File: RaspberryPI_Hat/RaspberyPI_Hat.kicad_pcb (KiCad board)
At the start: 2 copper layers, 65 x 56 mm, 45 parts, among them Q1 BC817, Q2 BC817, Q3 BC817, SW1 SW_PUSH, U1 CAT24C32WI-GT3

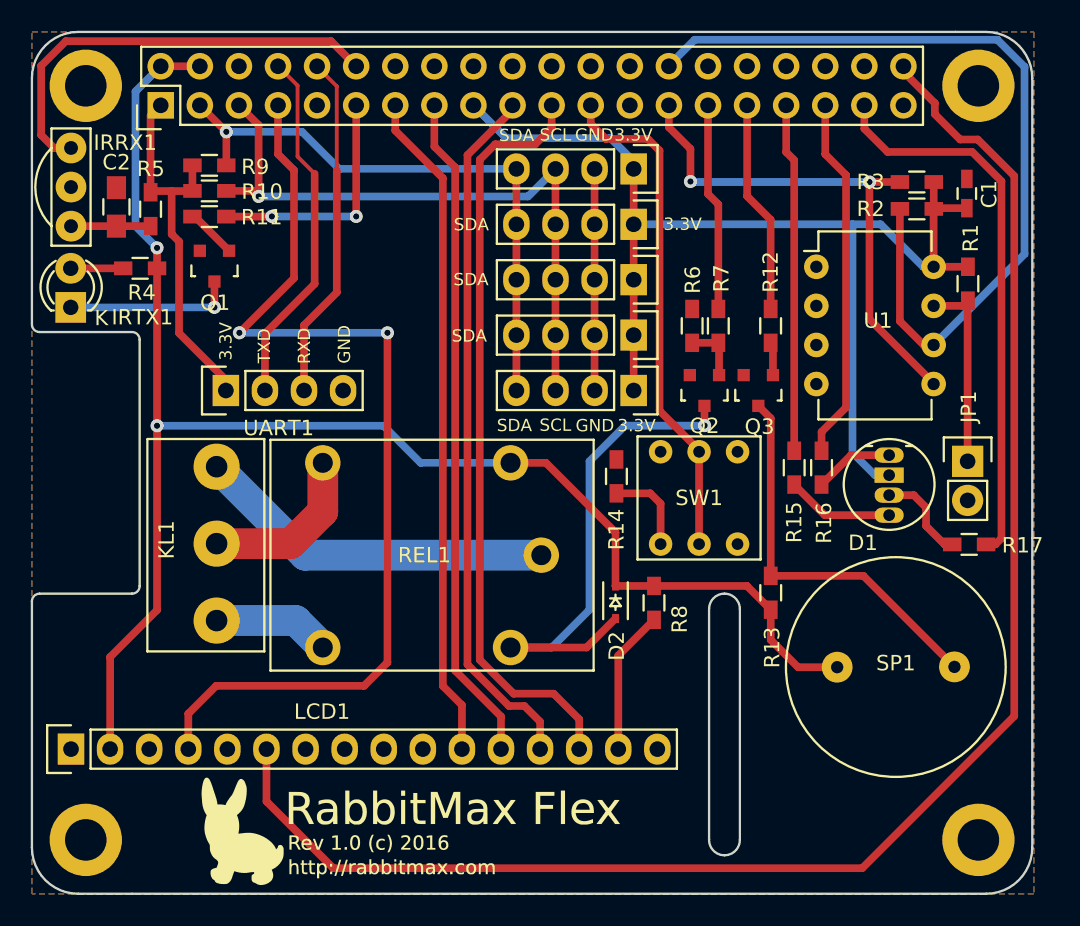
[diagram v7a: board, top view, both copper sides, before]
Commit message: changed common A to common Katode RGB LED
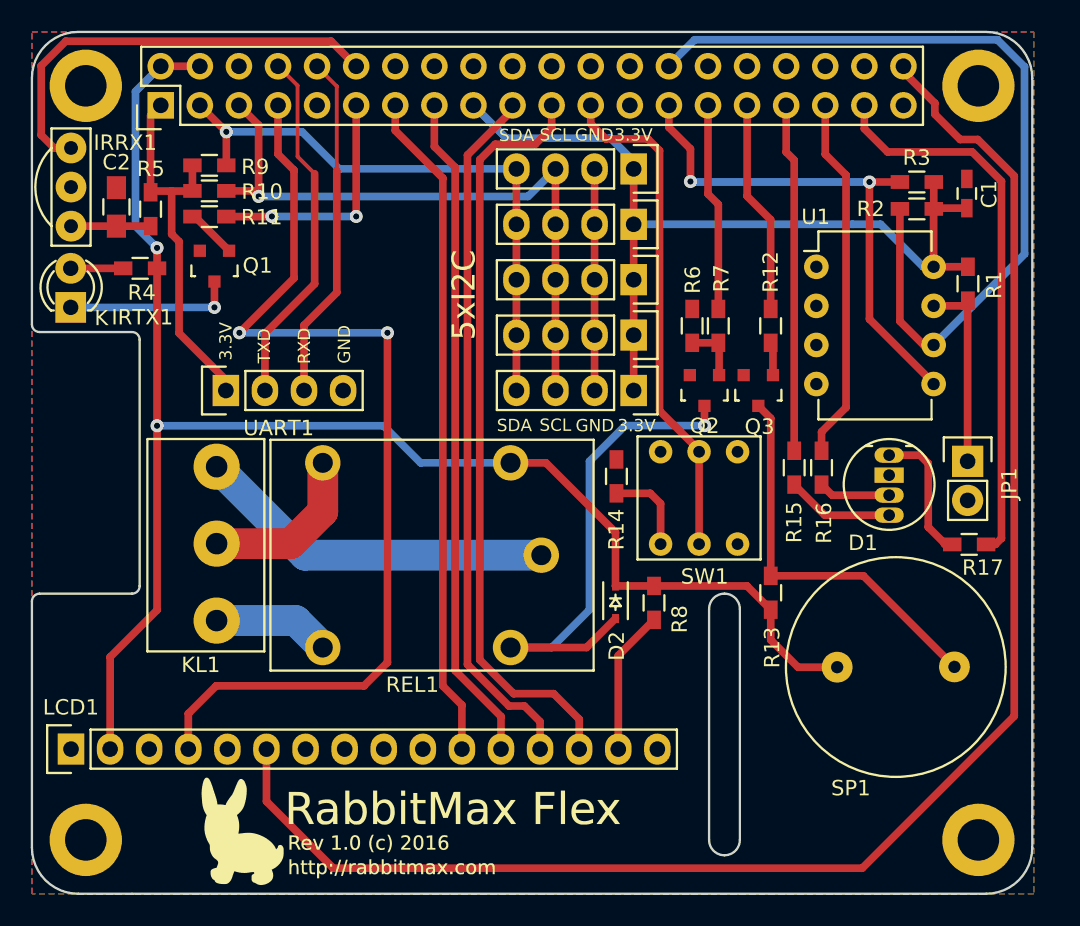
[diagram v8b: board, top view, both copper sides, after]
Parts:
- D1: value LED_RABG -> LED_RCBG
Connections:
- D1 pad 2: +3V3 -> GND
- R16 pad 2: Net-(D1-Pad1) -> Net-(D1-Pad3)
- R17 pad 1: Net-(D1-Pad3) -> Net-(D1-Pad1)
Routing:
- net +3V3: track 99.9 -> 82.1 mm
- net Net-(D1-Pad1): track 5.18 -> 9.42 mm
- net Net-(D1-Pad3): track 6.13 -> 4.68 mm
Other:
- board text added: "5xI2C"
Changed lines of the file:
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@@
     (links 110)
     (no_connects 2)
-    (area 97.924999 68.524999 163.075001 124.675001)
+    (area 86.242429 56.842428 174.757572 125.479)
     (thickness 1.6)
-    (drawings 44)
-    (tracks 265)
+    (drawings 41)
+    (tracks 263)
     (zones 0)
     (modules 45)
@@
       (effects (font (size 1 1) (thickness 0.15)))
     )
-    (fp_text value LED_RABG (at 0 6.25) (layer F.Fab)
+    (fp_text value LED_RCBG (at 0 6.25) (layer F.Fab)
       (effects (font (size 1 1) (thickness 0.15)))
     )
@@
       (net 43 "Net-(D1-Pad1)"))
     (pad 2 thru_hole rect (at 0 1.3) (size 1.905 1) (drill 0.762) (layers *.Cu *.Mask F.SilkS)
-      (net 2 +3V3))
+      (net 1 GND))
     (pad 3 thru_hole oval (at 0 2.6) (size 1.905 1) (drill 0.762) (layers *.Cu *.Mask F.SilkS)
       (net 44 "Net-(D1-Pad3)"))
@@
   (module myfootprint:PUSH_P1 (layer F.Cu)
     (at 141.35 98.88)
-    (fp_text reference SW1 (at 0 0) (layer F.SilkS)
+    (fp_text reference SW1 (at 0.36 5.11) (layer F.SilkS)
       (effects (font (size 1 1) (thickness 0.15)))
     )
@@
     (tags SOT-23)
     (attr smd)
-    (fp_text reference Q1 (at -0.04 -2.38 360) (layer F.SilkS)
+    (fp_text reference Q1 (at -2.8 0.04 360) (layer F.SilkS)
       (effects (font (size 1 1) (thickness 0.15)))
     )
@@
   (module myfootprint:PIEZO-MCKPI-G1410 (layer F.Cu)
     (at 154.134 109.868)
-    (fp_text reference SP1 (at 0 -0.25) (layer F.SilkS)
+    (fp_text reference SP1 (at -2.924 7.872) (layer F.SilkS)
       (effects (font (size 1 1) (thickness 0.15)))
     )
@@
     (tags "resistor 0603")
     (attr smd)
-    (fp_text reference R1 (at -2.96 -0.18 270) (layer F.SilkS)
+    (fp_text reference R1 (at 0.08 -1.7 270) (layer F.SilkS)
       (effects (font (size 1 1) (thickness 0.15)))
     )
@@
     (tags "resistor 0603")
     (attr smd)
-    (fp_text reference R3 (at 3 0 180) (layer F.SilkS)
+    (fp_text reference R3 (at 0.01 1.58 180) (layer F.SilkS)
       (effects (font (size 1 1) (thickness 0.15)))
     )
@@
     (descr "Through hole pin header")
     (tags "pin header")
-    (fp_text reference JP1 (at 0.08 -3.54 90) (layer F.SilkS)
+    (fp_text reference JP1 (at 2.71 1.46 90) (layer F.SilkS)
       (effects (font (size 1 1) (thickness 0.15)))
     )
@@
     (descr "8-lead dip package, row spacing 7.62 mm (300 mils)")
     (tags "dil dip 2.54 300")
-    (fp_text reference U1 (at 4 3.5) (layer F.SilkS)
+    (fp_text reference U1 (at -0.04 -3.24) (layer F.SilkS)
       (effects (font (size 1 1) (thickness 0.15)))
     )
@@
       (net 19 /LED1))
     (pad 2 smd rect (at 1.1 0 270) (size 1.2 0.9) (layers F.Cu F.Paste F.Mask)
-      (net 43 "Net-(D1-Pad1)"))
+      (net 44 "Net-(D1-Pad3)"))
     (model Resistors_SMD.3dshapes/R_0603_HandSoldering.wrl
       (at (xyz 0 0 0))
@@
   (module myfootprint:KLEMA_1x3 (layer F.Cu)
     (at 113.5 96.85 270)
-    (fp_text reference KL1 (at 4.75 6.75 270) (layer F.SilkS)
+    (fp_text reference KL1 (at 12.88 4.53 360) (layer F.SilkS)
       (effects (font (size 1 1) (thickness 0.15)))
     )
@@
   (module myfootprint:RAS-05-15 (layer F.Cu)
     (at 119 95.1)
-    (fp_text reference REL1 (at 4.5 7.5) (layer F.SilkS)
+    (fp_text reference REL1 (at 3.72 15.92) (layer F.SilkS)
       (effects (font (size 1 1) (thickness 0.15)))
     )
@@
     (descr "Through hole pin header")
     (tags "pin header")
-    (fp_text reference LCD1 (at 2.432 16.31 180) (layer F.SilkS)
+    (fp_text reference LCD1 (at 2.712 -0.01 180) (layer F.SilkS)
       (effects (font (size 1 1) (thickness 0.15)))
     )
@@
     (tags "resistor 0603")
     (attr smd)
-    (fp_text reference R17 (at 3.47 0.06) (layer F.SilkS)
+    (fp_text reference R17 (at 0.89 1.51) (layer F.SilkS)
       (effects (font (size 1 1) (thickness 0.15)))
     )
@@
     (fp_line (start -0.5 -0.675) (end 0.5 -0.675) (layer F.SilkS) (width 0.15))
     (pad 1 smd rect (at -1.1 0) (size 1.2 0.9) (layers F.Cu F.Paste F.Mask)
-      (net 44 "Net-(D1-Pad3)"))
+      (net 43 "Net-(D1-Pad1)"))
     (pad 2 smd rect (at 1.1 0) (size 1.2 0.9) (layers F.Cu F.Paste F.Mask)
       (net 46 /LED3))
@@
     )
   )
+  (gr_text 5xI2C (at 126.07 85.69 90) (layer F.SilkS)
+    (effects (font (size 1.5 1.5) (thickness 0.3)))
+  )
   (gr_text GND (at 134.54 75.29) (layer F.SilkS)
     (effects (font (size 0.8 0.8) (thickness 0.1)))
@@
     (effects (font (size 0.8 0.8) (thickness 0.1)))
   )
-  (gr_text 3.3V (at 140.28 81.09) (layer F.SilkS)
-    (effects (font (size 0.8 0.8) (thickness 0.1)))
-  )
   (gr_text 3.3V (at 137.09 75.29) (layer F.SilkS)
     (effects (font (size 0.8 0.8) (thickness 0.1)))
   )
   (gr_text SDA (at 129.49 75.32) (layer F.SilkS)
-    (effects (font (size 0.8 0.8) (thickness 0.1)))
-  )
-  (gr_text SDA (at 126.55 81.12) (layer F.SilkS)
-    (effects (font (size 0.8 0.8) (thickness 0.1)))
-  )
-  (gr_text SDA (at 126.53 84.69) (layer F.SilkS)
-    (effects (font (size 0.8 0.8) (thickness 0.1)))
-  )
-  (gr_text SDA (at 126.42 88.35) (layer F.SilkS)
     (effects (font (size 0.8 0.8) (thickness 0.1)))
   )
@@
   (segment (start 134.56 88.3) (end 134.56 91.9) (width 0.5) (layer F.Cu) (net 1) (status 30))
   (segment (start 134.56 88.3) (end 134.56 84.7) (width 0.5) (layer F.Cu) (net 1) (status 30))
-  (segment (start 153.7 97.4) (end 152.78 97.4) (width 0.5) (layer B.Cu) (net 2))
-  (segment (start 152.78 97.4) (end 151.32 95.94) (width 0.5) (layer B.Cu) (net 2))
-  (segment (start 151.32 95.94) (end 151.32 81.1) (width 0.5) (layer B.Cu) (net 2))
+  (segment (start 153.15 81.1) (end 151.32 81.1) (width 0.5) (layer B.Cu) (net 2))
   (segment (start 156.59 83.86) (end 155.91 83.86) (width 0.5) (layer B.Cu) (net 2))
   (segment (start 155.91 83.86) (end 153.15 81.1) (width 0.5) (layer B.Cu) (net 2))
-  (segment (start 153.15 81.1) (end 151.32 81.1) (width 0.5) (layer B.Cu) (net 2))
   (segment (start 151.32 81.1) (end 137.1 81.1) (width 0.5) (layer B.Cu) (net 2))
   (segment (start 108.43 77.27) (end 108.43 78.93) (width 0.5) (layer F.Cu) (net 2))
@@
   (segment (start 141.93 79.13) (end 141.93 73.37) (width 0.5) (layer F.Cu) (net 36))
   (segment (start 142.6 79.8) (end 141.93 79.13) (width 0.5) (layer F.Cu) (net 36))
-  (segment (start 153.7 96.1) (end 151.222 96.1) (width 0.5) (layer F.Cu) (net 43))
-  (segment (start 151.222 96.1) (end 149.308 98.014) (width 0.5) (layer F.Cu) (net 43))
-  (segment (start 157.8 101.9) (end 157.3 101.9) (width 0.5) (layer F.Cu) (net 44))
-  (segment (start 157.3 101.9) (end 156.1 100.7) (width 0.5) (layer F.Cu) (net 44))
-  (segment (start 156.1 100.7) (end 156.1 99.5) (width 0.5) (layer F.Cu) (net 44))
-  (segment (start 156.1 99.5) (end 155.3 98.7) (width 0.5) (layer F.Cu) (net 44))
-  (segment (start 155.3 98.7) (end 153.7 98.7) (width 0.5) (layer F.Cu) (net 44))
+  (segment (start 157.8 101.9) (end 157.37 101.9) (width 0.5) (layer F.Cu) (net 43))
+  (segment (start 157.37 101.9) (end 156.24 100.77) (width 0.5) (layer F.Cu) (net 43))
+  (segment (start 155.7 96.1) (end 153.7 96.1) (width 0.5) (layer F.Cu) (net 43))
+  (segment (start 156.24 96.64) (end 155.7 96.1) (width 0.5) (layer F.Cu) (net 43))
+  (segment (start 156.24 100.77) (end 156.24 96.64) (width 0.5) (layer F.Cu) (net 43))
+  (segment (start 157.8 101.9) (end 157.3 101.9) (width 0.5) (layer F.Cu) (net 43))
+  (segment (start 153.7 98.7) (end 149.994 98.7) (width 0.5) (layer F.Cu) (net 44))
+  (segment (start 149.994 98.7) (end 149.308 98.014) (width 0.5) (layer F.Cu) (net 44))
   (segment (start 153.7 100) (end 149.516 100) (width 0.5) (layer F.Cu) (net 45))
   (segment (start 149.516 100) (end 147.53 98.014) (width 0.5) (layer F.Cu) (net 45))
